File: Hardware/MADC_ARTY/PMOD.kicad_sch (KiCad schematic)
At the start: 2 parts, among them J3 71764-0012, J4 71764-0012

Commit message: Schematic
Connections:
- net AD_COMP: now reaches J4.12 (Pin_12)
- net FGPA_AD_IIN: now reaches J4.5 (Pin_5)
- net FGPA_AD_ID: now reaches J4.6 (Pin_6)
- net FGPA_AD_IRP: now reaches J4.7 (Pin_7)
- net FGPA_AD_IRN: now reaches J4.8 (Pin_8)
- net FPGA_SW_VRH: now reaches J4.9 (Pin_9)
- net GAIN_x10: now reaches J3.7 (Pin_7)
- net GAIN_x100: now reaches J3.8 (Pin_8)
- no-connect marks 4 -> 10
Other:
- moved on the sheet: J4
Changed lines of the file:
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@@
 	(paper "A4")
 	(no_connect
-		(at 172.72 78.74)
+		(at 180.34 78.74)
+	)
+	(no_connect
+		(at 125.73 91.44)
+	)
+	(no_connect
+		(at 167.64 91.44)
+	)
+	(no_connect
+		(at 180.34 88.9)
+	)
+	(no_connect
+		(at 113.03 88.9)
 	)
 	(no_connect
@@
 	)
 	(no_connect
-		(at 160.02 78.74)
+		(at 113.03 91.44)
+	)
+	(no_connect
+		(at 125.73 88.9)
+	)
+	(no_connect
+		(at 167.64 78.74)
 	)
 	(wire
@@
 	(wire
 		(pts
+			(xy 180.34 86.36) (xy 181.61 86.36)
+		)
+		(stroke
+			(width 0)
+			(type default)
+		)
+	)
+	(wire
+		(pts
+			(xy 180.34 91.44) (xy 181.61 91.44)
+		)
+		(stroke
+			(width 0)
+			(type default)
+		)
+	)
+	(wire
+		(pts
+			(xy 180.34 83.82) (xy 181.61 83.82)
+		)
+		(stroke
+			(width 0)
+			(type default)
+		)
+	)
+	(wire
+		(pts
 			(xy 125.73 83.82) (xy 127 83.82)
 		)
@@
 		)
 	)
+	(wire
+		(pts
+			(xy 125.73 86.36) (xy 127 86.36)
+		)
+		(stroke
+			(width 0)
+			(type default)
+		)
+	)
+	(wire
+		(pts
+			(xy 166.37 88.9) (xy 167.64 88.9)
+		)
+		(stroke
+			(width 0)
+			(type default)
+		)
+	)
+	(wire
+		(pts
+			(xy 166.37 83.82) (xy 167.64 83.82)
+		)
+		(stroke
+			(width 0)
+			(type default)
+		)
+	)
+	(wire
+		(pts
+			(xy 166.37 86.36) (xy 167.64 86.36)
+		)
+		(stroke
+			(width 0)
+			(type default)
+		)
+	)
+	(wire
+		(pts
+			(xy 111.76 86.36) (xy 113.03 86.36)
+		)
+		(stroke
+			(width 0)
+			(type default)
+		)
+	)
 	(hierarchical_label "AZ2_CTR"
 		(shape output)
@@
 		)
 	)
+	(hierarchical_label "FGPA_AD_ID"
+		(shape output)
+		(at 181.61 83.82 0)
+		(effects
+			(font
+				(size 1.27 1.27)
+			)
+			(justify left)
+		)
+	)
+	(hierarchical_label "FPGA_SW_VRH"
+		(shape output)
+		(at 166.37 88.9 180)
+		(effects
+			(font
+				(size 1.27 1.27)
+			)
+			(justify right)
+		)
+	)
 	(hierarchical_label "AZ1_CTR"
 		(shape output)
 		(at 111.76 83.82 180)
+		(effects
+			(font
+				(size 1.27 1.27)
+			)
+			(justify right)
+		)
+	)
+	(hierarchical_label "GAIN_x10"
+		(shape output)
+		(at 111.76 86.36 180)
+		(effects
+			(font
+				(size 1.27 1.27)
+			)
+			(justify right)
+		)
+	)
+	(hierarchical_label "GAIN_x100"
+		(shape output)
+		(at 127 86.36 0)
+		(effects
+			(font
+				(size 1.27 1.27)
+			)
+			(justify left)
+		)
+	)
+	(hierarchical_label "FGPA_AD_IRN"
+		(shape output)
+		(at 181.61 86.36 0)
+		(effects
+			(font
+				(size 1.27 1.27)
+			)
+			(justify left)
+		)
+	)
+	(hierarchical_label "FGPA_AD_IRP"
+		(shape output)
+		(at 166.37 86.36 180)
+		(effects
+			(font
+				(size 1.27 1.27)
+			)
+			(justify right)
+		)
+	)
+	(hierarchical_label "AD_COMP"
+		(shape input)
+		(at 181.61 91.44 0)
+		(effects
+			(font
+				(size 1.27 1.27)
+			)
+			(justify left)
+		)
+	)
+	(hierarchical_label "FGPA_AD_IIN"
+		(shape output)
+		(at 166.37 83.82 180)
 		(effects
 			(font
@@
 	(symbol
 		(lib_id "power:GND")
-		(at 172.72 81.28 90)
+		(at 180.34 81.28 90)
 		(mirror x)
 		(unit 1)
@@
 		(fields_autoplaced yes)
 		(property "Reference" "#PWR0151"
-			(at 179.07 81.28 0)
+			(at 186.69 81.28 0)
 			(effects
 				(font
@@
 		)
 		(property "Value" "GND"
-			(at 175.895 81.28 90)
+			(at 183.515 81.28 90)
 			(effects
 				(font
@@
 		)
 		(property "Footprint" ""
-			(at 172.72 81.28 0)
+			(at 180.34 81.28 0)
 			(effects
 				(font
@@
 		)
 		(property "Datasheet" ""
-			(at 172.72 81.28 0)
+			(at 180.34 81.28 0)
 			(effects
 				(font
@@
 		)
 		(property "Description" ""
-			(at 172.72 81.28 0)
+			(at 180.34 81.28 0)
 			(effects
 				(font
@@
 	(symbol
 		(lib_id "power:GND")
-		(at 160.02 81.28 270)
+		(at 167.64 81.28 270)
 		(mirror x)
 		(unit 1)
@@
 		(fields_autoplaced yes)
 		(property "Reference" "#PWR0149"
-			(at 153.67 81.28 0)
+			(at 161.29 81.28 0)
 			(effects
 				(font
@@
 		)
 		(property "Value" "GND"
-			(at 156.845 81.28 90)
+			(at 164.465 81.28 90)
 			(effects
 				(font
@@
 		)
 		(property "Footprint" ""
-			(at 160.02 81.28 0)
+			(at 167.64 81.28 0)
 			(effects
 				(font
@@
 		)
 		(property "Datasheet" ""
-			(at 160.02 81.28 0)
+			(at 167.64 81.28 0)
 			(effects
 				(font
@@
 		)
 		(property "Description" ""
-			(at 160.02 81.28 0)
+			(at 167.64 81.28 0)
 			(effects
 				(font
@@
 	(symbol
 		(lib_id "Connector_Generic:Conn_02x06_Odd_Even")
-		(at 165.1 83.82 0)
+		(at 172.72 83.82 0)
 		(unit 1)
 		(exclude_from_sim no)
@@
 		(fields_autoplaced yes)
 		(property "Reference" "J4"
-			(at 166.37 73.025 0)
+			(at 173.99 73.025 0)
 			(effects
 				(font
@@
 		)
 		(property "Value" "71764-0012"
-			(at 166.37 75.565 0)
+			(at 173.99 75.565 0)
 			(effects
 				(font
@@
 		)
 		(property "Footprint" "Connector_PinHeader_2.54mm:PinHeader_2x06_P2.54mm_Horizontal"
-			(at 165.1 83.82 0)
+			(at 172.72 83.82 0)
 			(effects
 				(font
@@
 		)
 		(property "Datasheet" "~"
-			(at 165.1 83.82 0)
+			(at 172.72 83.82 0)
 			(effects
 				(font
@@
 		)
 		(property "Description" ""
-			(at 165.1 83.82 0)
-			(effects
-				(font
+			(at 172.72 83.82 0)
+			(effects
+				(font

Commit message: Schematic
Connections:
- net AD_COMP: now also J4.10 (Pin_10); no longer J4.12 (Pin_12)
- net GAIN_x10: now also J4.11 (Pin_11); no longer J3.7 (Pin_7)
- net GAIN_x100: now also J4.12 (Pin_12); no longer J3.8 (Pin_8)
- net AZ1_CTR renamed AZ_CTR
- net AZ2_CTR: no longer names the net of J3.6 (Pin_6)
- no-connect marks 10 -> 11
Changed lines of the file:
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@@
 	)
 	(no_connect
-		(at 167.64 91.44)
+		(at 113.03 86.36)
 	)
 	(no_connect
-		(at 180.34 88.9)
+		(at 125.73 86.36)
 	)
 	(no_connect
 		(at 113.03 88.9)
+	)
+	(no_connect
+		(at 125.73 83.82)
 	)
 	(no_connect
@@
 	(wire
 		(pts
+			(xy 166.37 91.44) (xy 167.64 91.44)
+		)
+		(stroke
+			(width 0)
+			(type default)
+		)
+	)
+	(wire
+		(pts
 			(xy 180.34 86.36) (xy 181.61 86.36)
 		)
@@
 	(wire
 		(pts
-			(xy 180.34 91.44) (xy 181.61 91.44)
+			(xy 180.34 88.9) (xy 181.61 88.9)
 		)
 		(stroke
@@
 	(wire
 		(pts
-			(xy 125.73 83.82) (xy 127 83.82)
-		)
-		(stroke
-			(width 0)
-			(type default)
-		)
-	)
-	(wire
-		(pts
-			(xy 125.73 86.36) (xy 127 86.36)
+			(xy 180.34 91.44) (xy 181.61 91.44)
 		)
 		(stroke
@@
 		)
 	)
-	(wire
-		(pts
-			(xy 111.76 86.36) (xy 113.03 86.36)
-		)
-		(stroke
-			(width 0)
-			(type default)
-		)
-	)
-	(hierarchical_label "AZ2_CTR"
-		(shape output)
-		(at 127 83.82 0)
-		(effects
-			(font
-				(size 1.27 1.27)
-			)
-			(justify left)
-		)
-	)
 	(hierarchical_label "FGPA_AD_ID"
 		(shape output)
@@
 		)
 	)
-	(hierarchical_label "AZ1_CTR"
+	(hierarchical_label "AZ_CTR"
 		(shape output)
 		(at 111.76 83.82 180)
@@
 	(hierarchical_label "GAIN_x10"
 		(shape output)
-		(at 111.76 86.36 180)
+		(at 166.37 91.44 180)
 		(effects
 			(font
@@
 	(hierarchical_label "GAIN_x100"
 		(shape output)
-		(at 127 86.36 0)
+		(at 181.61 91.44 0)
 		(effects
 			(font
@@
 	(hierarchical_label "AD_COMP"
 		(shape input)
-		(at 181.61 91.44 0)
+		(at 181.61 88.9 0)
 		(effects
 			(font

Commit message: PCB and Schematic
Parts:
- added TP31, TP32, TP33, TP34, TP35, TP36, TP37, TP38, TP39: TestPoint, symbol Connector:TestPoint
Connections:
- net AD_COMP: now also TP38.1
- net AZ_CTR: now also TP31.1
- net FGPA_AD_ID: now also TP36.1
- net FGPA_AD_IIN: now also TP32.1
- net FGPA_AD_IRN: now also TP37.1
- net FGPA_AD_IRP: now also TP33.1
- net FPGA_SW_VRH: now also TP34.1
- net GAIN_x10: now also TP35.1
- net GAIN_x100: now also TP39.1
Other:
- moved on the sheet: J4

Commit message: PCB
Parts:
- TP24: renamed from TP31; footprint (none) -> TestPoint:TestPoint_Pad_D2.0mm
- TP25: renamed from TP32; footprint (none) -> TestPoint:TestPoint_Pad_D2.0mm
- TP26: renamed from TP34; footprint (none) -> TestPoint:TestPoint_Pad_D2.0mm
- TP27: renamed from TP33; footprint (none) -> TestPoint:TestPoint_Pad_D2.0mm
- TP28: renamed from TP35; footprint (none) -> TestPoint:TestPoint_Pad_D2.0mm
- TP29: renamed from TP36; footprint (none) -> TestPoint:TestPoint_Pad_D2.0mm
- TP30: renamed from TP38; footprint (none) -> TestPoint:TestPoint_Pad_D2.0mm
- TP31: renamed from TP37; footprint (none) -> TestPoint:TestPoint_Pad_D2.0mm
- TP32: renamed from TP39; footprint (none) -> TestPoint:TestPoint_Pad_D2.0mm
- renumbered J3 to J4, J4 to J5
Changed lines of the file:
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@@
 		(dnp no)
 		(fields_autoplaced yes)
-		(property "Reference" "TP36"
+		(property "Reference" "TP29"
 			(at 213.36 75.4379 0)
 			(effects
@@
 			)
 		)
-		(property "Footprint" ""
+		(property "Footprint" "TestPoint:TestPoint_Pad_D2.0mm"
 			(at 215.9 80.01 0)
 			(effects
@@
 			(project "MADC_ARTY"
 				(path "/eadab778-ea7c-433e-b0bd-0d0c238907e0/37dfacfc-f3f5-4a09-9e7e-ab0b8ea302f6/5d4b0f99-b739-4f3c-9f1e-19d2c8b0b121"
-					(reference "TP36")
+					(reference "TP29")
 					(unit 1)
 				)
@@
 		(dnp no)
 		(fields_autoplaced yes)
-		(property "Reference" "TP38"
+		(property "Reference" "TP30"
 			(at 213.36 99.8221 0)
 			(effects
@@
 			)
 		)
-		(property "Footprint" ""
+		(property "Footprint" "TestPoint:TestPoint_Pad_D2.0mm"
 			(at 215.9 95.25 0)
 			(effects
@@
 			(project "MADC_ARTY"
 				(path "/eadab778-ea7c-433e-b0bd-0d0c238907e0/37dfacfc-f3f5-4a09-9e7e-ab0b8ea302f6/5d4b0f99-b739-4f3c-9f1e-19d2c8b0b121"
-					(reference "TP38")
+					(reference "TP30")
 					(unit 1)
 				)
@@
 		(dnp no)
 		(fields_autoplaced yes)
-		(property "Reference" "TP31"
+		(property "Reference" "TP24"
 			(at 93.98 77.9779 0)
 			(effects
@@
 			)
 		)
-		(property "Footprint" ""
+		(property "Footprint" "TestPoint:TestPoint_Pad_D2.0mm"
 			(at 96.52 82.55 0)
 			(effects
@@
 			(project "MADC_ARTY"
 				(path "/eadab778-ea7c-433e-b0bd-0d0c238907e0/37dfacfc-f3f5-4a09-9e7e-ab0b8ea302f6/5d4b0f99-b739-4f3c-9f1e-19d2c8b0b121"
-					(reference "TP31")
+					(reference "TP24")
 					(unit 1)
 				)
@@
 		(dnp no)
 		(fields_autoplaced yes)
-		(property "Reference" "#PWR0133"
+		(property "Reference" "#PWR0139"
 			(at 208.28 81.28 0)
 			(effects
@@
 			(project "MADC_ARTY"
 				(path "/eadab778-ea7c-433e-b0bd-0d0c238907e0/37dfacfc-f3f5-4a09-9e7e-ab0b8ea302f6/5d4b0f99-b739-4f3c-9f1e-19d2c8b0b121"
-					(reference "#PWR0133")
+					(reference "#PWR0139")
 					(unit 1)
 				)
@@
 		(dnp no)
 		(fields_autoplaced yes)
-		(property "Reference" "TP33"
+		(property "Reference" "TP27"
 			(at 176.53 75.4379 0)
 			(effects
@@
 			)
 		)
-		(property "Footprint" ""
+		(property "Footprint" "TestPoint:TestPoint_Pad_D2.0mm"
 			(at 179.07 80.01 0)
 			(effects
@@
 			(project "MADC_ARTY"
 				(path "/eadab778-ea7c-433e-b0bd-0d0c238907e0/37dfacfc-f3f5-4a09-9e7e-ab0b8ea302f6/5d4b0f99-b739-4f3c-9f1e-19d2c8b0b121"
-					(reference "TP33")
+					(reference "TP27")
 					(unit 1)
 				)
@@
 		(dnp no)
 		(fields_autoplaced yes)
-		(property "Reference" "TP32"
+		(property "Reference" "TP25"
 			(at 163.83 75.4379 0)
 			(effects
@@
 			)
 		)
-		(property "Footprint" ""
+		(property "Footprint" "TestPoint:TestPoint_Pad_D2.0mm"
 			(at 166.37 80.01 0)
 			(effects
@@
 			(project "MADC_ARTY"
 				(path "/eadab778-ea7c-433e-b0bd-0d0c238907e0/37dfacfc-f3f5-4a09-9e7e-ab0b8ea302f6/5d4b0f99-b739-4f3c-9f1e-19d2c8b0b121"
-					(reference "TP32")
+					(reference "TP25")
 					(unit 1)
 				)
@@
 		(dnp no)
 		(fields_autoplaced yes)
-		(property "Reference" "#PWR0130"
+		(property "Reference" "#PWR0136"
 			(at 106.68 81.28 0)
 			(effects
@@
 			(project "MADC_ARTY"
 				(path "/eadab778-ea7c-433e-b0bd-0d0c238907e0/37dfacfc-f3f5-4a09-9e7e-ab0b8ea302f6/5d4b0f99-b739-4f3c-9f1e-19d2c8b0b121"
-					(reference "#PWR0130")
+					(reference "#PWR0136")
 					(unit 1)
 				)
@@
 		(dnp no)
 		(fields_autoplaced yes)
-		(property "Reference" "#PWR0132"
+		(property "Reference" "#PWR0138"
 			(at 182.88 81.28 0)
 			(effects
@@
 			(project "MADC_ARTY"
 				(path "/eadab778-ea7c-433e-b0bd-0d0c238907e0/37dfacfc-f3f5-4a09-9e7e-ab0b8ea302f6/5d4b0f99-b739-4f3c-9f1e-19d2c8b0b121"
-					(reference "#PWR0132")
+					(reference "#PWR0138")
 					(unit 1)
 				)
@@
 		(dnp no)
 		(fields_autoplaced yes)
-		(property "Reference" "J4"
+		(property "Reference" "J5"
 			(at 195.58 73.025 0)
 			(effects
@@
 			(project "MADC_ARTY"
 				(path "/eadab778-ea7c-433e-b0bd-0d0c238907e0/37dfacfc-f3f5-4a09-9e7e-ab0b8ea302f6/5d4b0f99-b739-4f3c-9f1e-19d2c8b0b121"
-					(reference "J4")
+					(reference "J5")
 					(unit 1)
 				)
@@
 		(dnp no)
 		(fields_autoplaced yes)
-		(property "Reference" "#PWR0131"
+		(property "Reference" "#PWR0137"
 			(at 132.08 81.28 0)
 			(effects
@@
 			(project "MADC_ARTY"
 				(path "/eadab778-ea7c-433e-b0bd-0d0c238907e0/37dfacfc-f3f5-4a09-9e7e-ab0b8ea302f6/5d4b0f99-b739-4f3c-9f1e-19d2c8b0b121"
-					(reference "#PWR0131")
+					(reference "#PWR0137")
 					(unit 1)
 				)
@@
 		(dnp no)
 		(fields_autoplaced yes)
-		(property "Reference" "TP34"
+		(property "Reference" "TP26"
 			(at 163.83 97.2819 0)
 			(effects
@@
 			)
 		)
-		(property "Footprint" ""
+		(property "Footprint" "TestPoint:TestPoint_Pad_D2.0mm"
 			(at 156.21 95.25 0)
 			(effects
@@
 			(project "MADC_ARTY"
 				(path "/eadab778-ea7c-433e-b0bd-0d0c238907e0/37dfacfc-f3f5-4a09-9e7e-ab0b8ea302f6/5d4b0f99-b739-4f3c-9f1e-19d2c8b0b121"
-					(reference "TP34")
+					(reference "TP26")
 					(unit 1)
 				)
@@
 		(dnp no)
 		(fields_autoplaced yes)
-		(property "Reference" "TP37"
+		(property "Reference" "TP31"
 			(at 226.06 75.4379 0)
 			(effects
@@
 			)
 		)
-		(property "Footprint" ""
+		(property "Footprint" "TestPoint:TestPoint_Pad_D2.0mm"
 			(at 228.6 80.01 0)
 			(effects
@@
 			(project "MADC_ARTY"
 				(path "/eadab778-ea7c-433e-b0bd-0d0c238907e0/37dfacfc-f3f5-4a09-9e7e-ab0b8ea302f6/5d4b0f99-b739-4f3c-9f1e-19d2c8b0b121"
-					(reference "TP37")
+					(reference "TP31")
 					(unit 1)
 				)
@@
 		(on_board yes)
 		(dnp no)
-		(property "Reference" "J3"
+		(property "Reference" "J4"
 			(at 119.38 73.025 0)
 			(effects
@@
 			(project "MADC_ARTY"
 				(path "/eadab778-ea7c-433e-b0bd-0d0c238907e0/37dfacfc-f3f5-4a09-9e7e-ab0b8ea302f6/5d4b0f99-b739-4f3c-9f1e-19d2c8b0b121"
-					(reference "J3")
+					(reference "J4")
 					(unit 1)
 				)
@@
 		(dnp no)
 		(fields_autoplaced yes)
-		(property "Reference" "TP35"
+		(property "Reference" "TP28"
 			(at 176.53 97.2819 0)
 			(effects
@@
 			)
 		)
-		(property "Footprint" ""
+		(property "Footprint" "TestPoint:TestPoint_Pad_D2.0mm"
 			(at 168.91 95.25 0)
 			(effects
@@
 			(project "MADC_ARTY"
 				(path "/eadab778-ea7c-433e-b0bd-0d0c238907e0/37dfacfc-f3f5-4a09-9e7e-ab0b8ea302f6/5d4b0f99-b739-4f3c-9f1e-19d2c8b0b121"
-					(reference "TP35")
+					(reference "TP28")
 					(unit 1)
 				)
@@
 		(dnp no)
 		(fields_autoplaced yes)
-		(property "Reference" "TP39"
+		(property "Reference" "TP32"
 			(at 226.06 99.8221 0)
 			(effects
@@
 			)
 		)
-		(property "Footprint" ""
+		(property "Footprint" "TestPoint:TestPoint_Pad_D2.0mm"
 			(at 228.6 95.25 0)
 			(effects
@@
 			(project "MADC_ARTY"
 				(path "/eadab778-ea7c-433e-b0bd-0d0c238907e0/37dfacfc-f3f5-4a09-9e7e-ab0b8ea302f6/5d4b0f99-b739-4f3c-9f1e-19d2c8b0b121"
-					(reference "TP39")
-					(unit 1)
-				)
+					(reference "TP32")
+					(unit 1)
+				)

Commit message: Schematic
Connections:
- net AD_COMP: now also J5.6 (Pin_6), TP29.1; no longer J5.10 (Pin_10), TP30.1
- net FGPA_AD_ID: now also J5.5 (Pin_5), TP25.1; no longer J5.6 (Pin_6), TP29.1
- net FGPA_AD_IIN: now also J5.10 (Pin_10), TP30.1; no longer J5.5 (Pin_5), TP25.1
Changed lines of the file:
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@@
 	(hierarchical_label "FGPA_AD_ID"
 		(shape output)
-		(at 234.95 83.82 0)
+		(at 158.75 83.82 180)
 		(effects
 			(font
 				(size 1.27 1.27)
 			)
-			(justify left)
+			(justify right)
 		)
 	)
@@
 	(hierarchical_label "AD_COMP"
 		(shape input)
-		(at 234.95 88.9 0)
+		(at 234.95 83.82 0)
 		(effects
 			(font
@@
 	(hierarchical_label "FGPA_AD_IIN"
 		(shape output)
-		(at 158.75 83.82 180)
+		(at 234.95 88.9 0)
 		(effects
 			(font
 				(size 1.27 1.27)
 			)
-			(justify right)
+			(justify left)
 		)
 	)

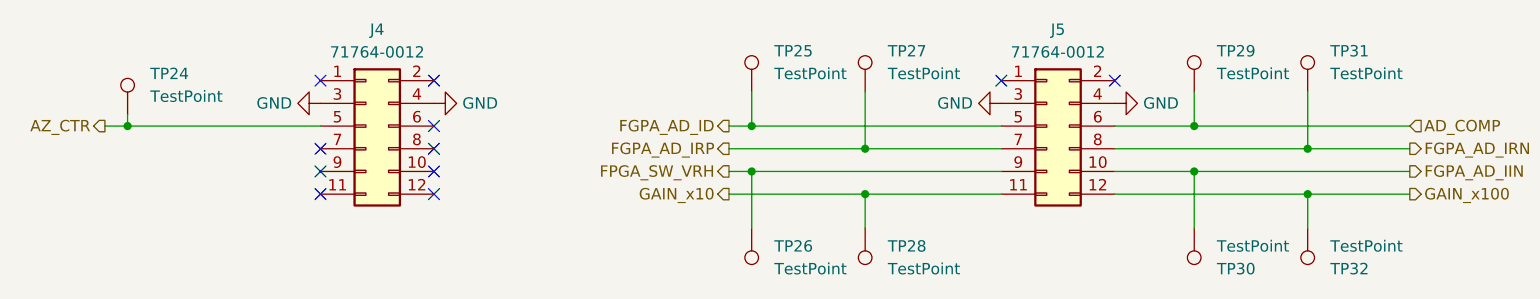
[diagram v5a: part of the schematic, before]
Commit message: MADC module send to production
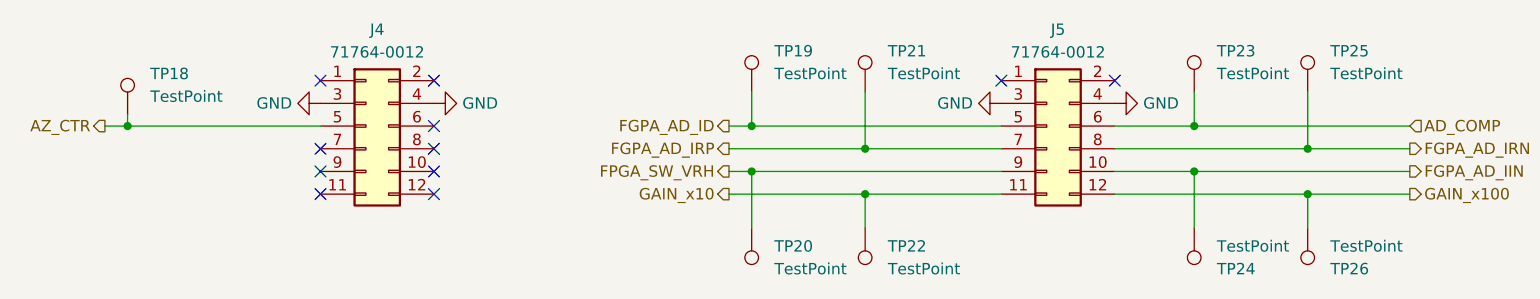
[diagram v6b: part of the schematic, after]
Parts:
- renumbered TP24 to TP18, TP25 to TP19, TP26 to TP20, TP27 to TP21, TP28 to TP22, TP29 to TP23, TP30 to TP24, TP31 to TP25, TP32 to TP26
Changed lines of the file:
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@@
 		(dnp no)
 		(fields_autoplaced yes)
-		(property "Reference" "TP29"
+		(property "Reference" "TP23"
 			(at 213.36 75.4379 0)
 			(effects
@@
 			(project "MADC_ARTY"
 				(path "/eadab778-ea7c-433e-b0bd-0d0c238907e0/37dfacfc-f3f5-4a09-9e7e-ab0b8ea302f6/5d4b0f99-b739-4f3c-9f1e-19d2c8b0b121"
-					(reference "TP29")
+					(reference "TP23")
 					(unit 1)
 				)
@@
 		(dnp no)
 		(fields_autoplaced yes)
-		(property "Reference" "TP30"
+		(property "Reference" "TP24"
 			(at 213.36 99.8221 0)
 			(effects
@@
 			(project "MADC_ARTY"
 				(path "/eadab778-ea7c-433e-b0bd-0d0c238907e0/37dfacfc-f3f5-4a09-9e7e-ab0b8ea302f6/5d4b0f99-b739-4f3c-9f1e-19d2c8b0b121"
-					(reference "TP30")
+					(reference "TP24")
 					(unit 1)
 				)
@@
 		(dnp no)
 		(fields_autoplaced yes)
-		(property "Reference" "TP24"
+		(property "Reference" "TP18"
 			(at 93.98 77.9779 0)
 			(effects
@@
 			(project "MADC_ARTY"
 				(path "/eadab778-ea7c-433e-b0bd-0d0c238907e0/37dfacfc-f3f5-4a09-9e7e-ab0b8ea302f6/5d4b0f99-b739-4f3c-9f1e-19d2c8b0b121"
-					(reference "TP24")
+					(reference "TP18")
 					(unit 1)
 				)
@@
 		(dnp no)
 		(fields_autoplaced yes)
-		(property "Reference" "#PWR0139"
+		(property "Reference" "#PWR0103"
 			(at 208.28 81.28 0)
 			(effects
@@
 			(project "MADC_ARTY"
 				(path "/eadab778-ea7c-433e-b0bd-0d0c238907e0/37dfacfc-f3f5-4a09-9e7e-ab0b8ea302f6/5d4b0f99-b739-4f3c-9f1e-19d2c8b0b121"
-					(reference "#PWR0139")
+					(reference "#PWR0103")
 					(unit 1)
 				)
@@
 		(dnp no)
 		(fields_autoplaced yes)
-		(property "Reference" "TP27"
+		(property "Reference" "TP21"
 			(at 176.53 75.4379 0)
 			(effects
@@
 			(project "MADC_ARTY"
 				(path "/eadab778-ea7c-433e-b0bd-0d0c238907e0/37dfacfc-f3f5-4a09-9e7e-ab0b8ea302f6/5d4b0f99-b739-4f3c-9f1e-19d2c8b0b121"
-					(reference "TP27")
+					(reference "TP21")
 					(unit 1)
 				)
@@
 		(dnp no)
 		(fields_autoplaced yes)
-		(property "Reference" "TP25"
+		(property "Reference" "TP19"
 			(at 163.83 75.4379 0)
 			(effects
@@
 			(project "MADC_ARTY"
 				(path "/eadab778-ea7c-433e-b0bd-0d0c238907e0/37dfacfc-f3f5-4a09-9e7e-ab0b8ea302f6/5d4b0f99-b739-4f3c-9f1e-19d2c8b0b121"
-					(reference "TP25")
+					(reference "TP19")
 					(unit 1)
 				)
@@
 		(dnp no)
 		(fields_autoplaced yes)
-		(property "Reference" "#PWR0136"
+		(property "Reference" "#PWR0100"
 			(at 106.68 81.28 0)
 			(effects
@@
 			(project "MADC_ARTY"
 				(path "/eadab778-ea7c-433e-b0bd-0d0c238907e0/37dfacfc-f3f5-4a09-9e7e-ab0b8ea302f6/5d4b0f99-b739-4f3c-9f1e-19d2c8b0b121"
-					(reference "#PWR0136")
+					(reference "#PWR0100")
 					(unit 1)
 				)
@@
 		(dnp no)
 		(fields_autoplaced yes)
-		(property "Reference" "#PWR0138"
+		(property "Reference" "#PWR0102"
 			(at 182.88 81.28 0)
 			(effects
@@
 			(project "MADC_ARTY"
 				(path "/eadab778-ea7c-433e-b0bd-0d0c238907e0/37dfacfc-f3f5-4a09-9e7e-ab0b8ea302f6/5d4b0f99-b739-4f3c-9f1e-19d2c8b0b121"
-					(reference "#PWR0138")
+					(reference "#PWR0102")
 					(unit 1)
 				)
@@
 		(dnp no)
 		(fields_autoplaced yes)
-		(property "Reference" "#PWR0137"
+		(property "Reference" "#PWR0101"
 			(at 132.08 81.28 0)
 			(effects
@@
 			(project "MADC_ARTY"
 				(path "/eadab778-ea7c-433e-b0bd-0d0c238907e0/37dfacfc-f3f5-4a09-9e7e-ab0b8ea302f6/5d4b0f99-b739-4f3c-9f1e-19d2c8b0b121"
-					(reference "#PWR0137")
+					(reference "#PWR0101")
 					(unit 1)
 				)
@@
 		(dnp no)
 		(fields_autoplaced yes)
-		(property "Reference" "TP26"
+		(property "Reference" "TP20"
 			(at 163.83 97.2819 0)
 			(effects
@@
 			(project "MADC_ARTY"
 				(path "/eadab778-ea7c-433e-b0bd-0d0c238907e0/37dfacfc-f3f5-4a09-9e7e-ab0b8ea302f6/5d4b0f99-b739-4f3c-9f1e-19d2c8b0b121"
-					(reference "TP26")
+					(reference "TP20")
 					(unit 1)
 				)
@@
 		(dnp no)
 		(fields_autoplaced yes)
-		(property "Reference" "TP31"
+		(property "Reference" "TP25"
 			(at 226.06 75.4379 0)
 			(effects
@@
 			(project "MADC_ARTY"
 				(path "/eadab778-ea7c-433e-b0bd-0d0c238907e0/37dfacfc-f3f5-4a09-9e7e-ab0b8ea302f6/5d4b0f99-b739-4f3c-9f1e-19d2c8b0b121"
-					(reference "TP31")
+					(reference "TP25")
 					(unit 1)
 				)
@@
 		(dnp no)
 		(fields_autoplaced yes)
-		(property "Reference" "TP28"
+		(property "Reference" "TP22"
 			(at 176.53 97.2819 0)
 			(effects
@@
 			(project "MADC_ARTY"
 				(path "/eadab778-ea7c-433e-b0bd-0d0c238907e0/37dfacfc-f3f5-4a09-9e7e-ab0b8ea302f6/5d4b0f99-b739-4f3c-9f1e-19d2c8b0b121"
-					(reference "TP28")
+					(reference "TP22")
 					(unit 1)
 				)
@@
 		(dnp no)
 		(fields_autoplaced yes)
-		(property "Reference" "TP32"
+		(property "Reference" "TP26"
 			(at 226.06 99.8221 0)
 			(effects
@@
 			(project "MADC_ARTY"
 				(path "/eadab778-ea7c-433e-b0bd-0d0c238907e0/37dfacfc-f3f5-4a09-9e7e-ab0b8ea302f6/5d4b0f99-b739-4f3c-9f1e-19d2c8b0b121"
-					(reference "TP32")
-					(unit 1)
-				)
+					(reference "TP26")
+					(unit 1)
+				)
